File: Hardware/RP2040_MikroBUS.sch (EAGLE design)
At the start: 76 parts, among them J1 SWD, J3 Qwiic, J5 USB C, J6 microSD, J9 MIKROBUS_SMD_BLACK1, Q1 20V/4.2A/52mΩ/1.4W, U2 MAX17048, U3 MCP73831, U4 W25QXX128MBIT, U5 RP2040, U6 WS2812-2020, U7 3.3V, Y2 12MHz

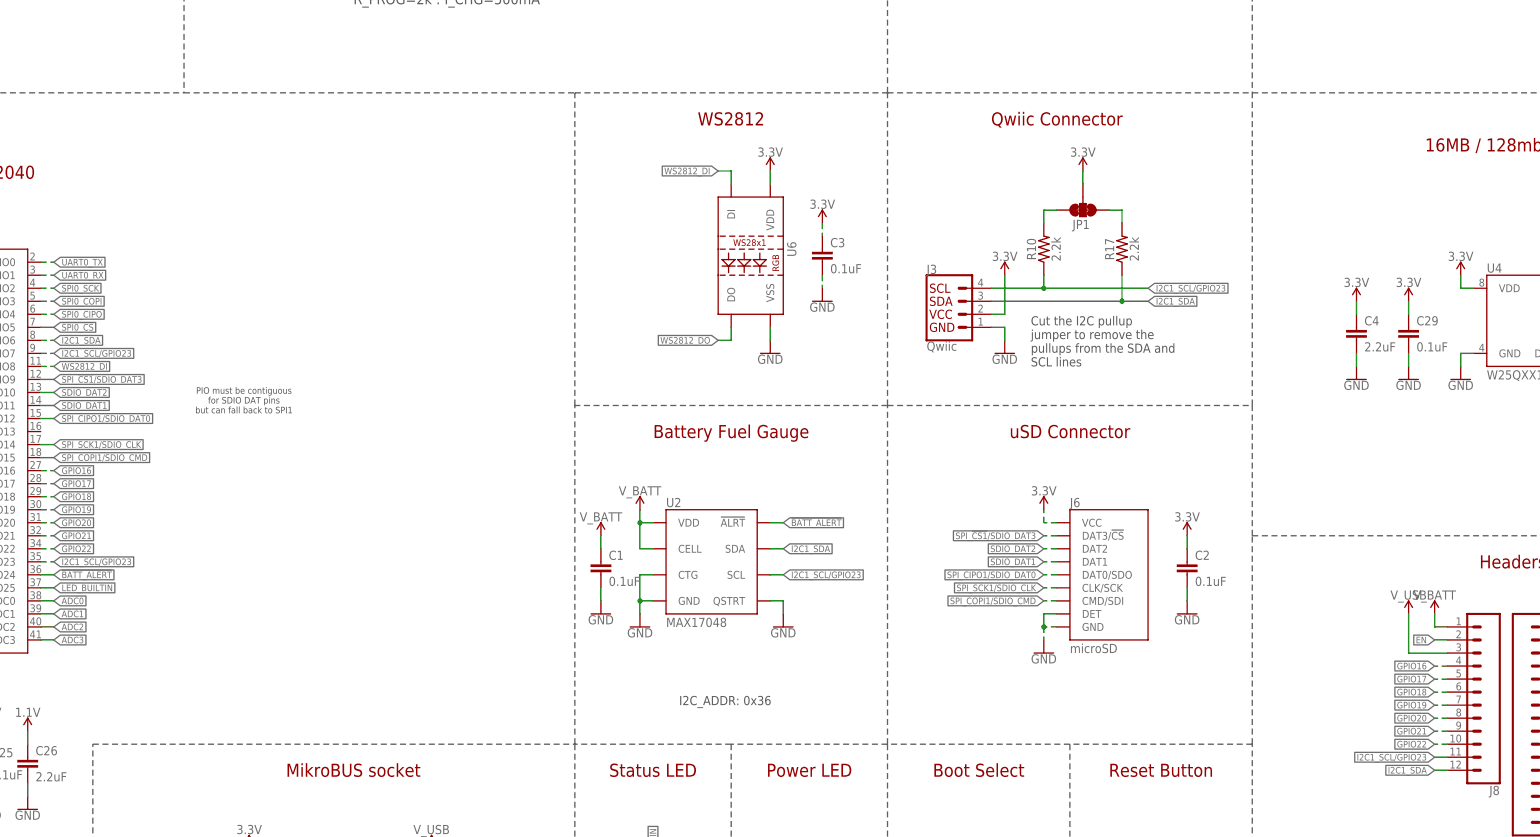
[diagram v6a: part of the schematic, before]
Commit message: Board updates
* Fix RESET button label
* Add RP2040 to SF microcontroller library and update in sch/board
* Gave some more space between the new traces I placed
* Brought D+ and D- traces closer together
* Changed "WS2812" label to text only
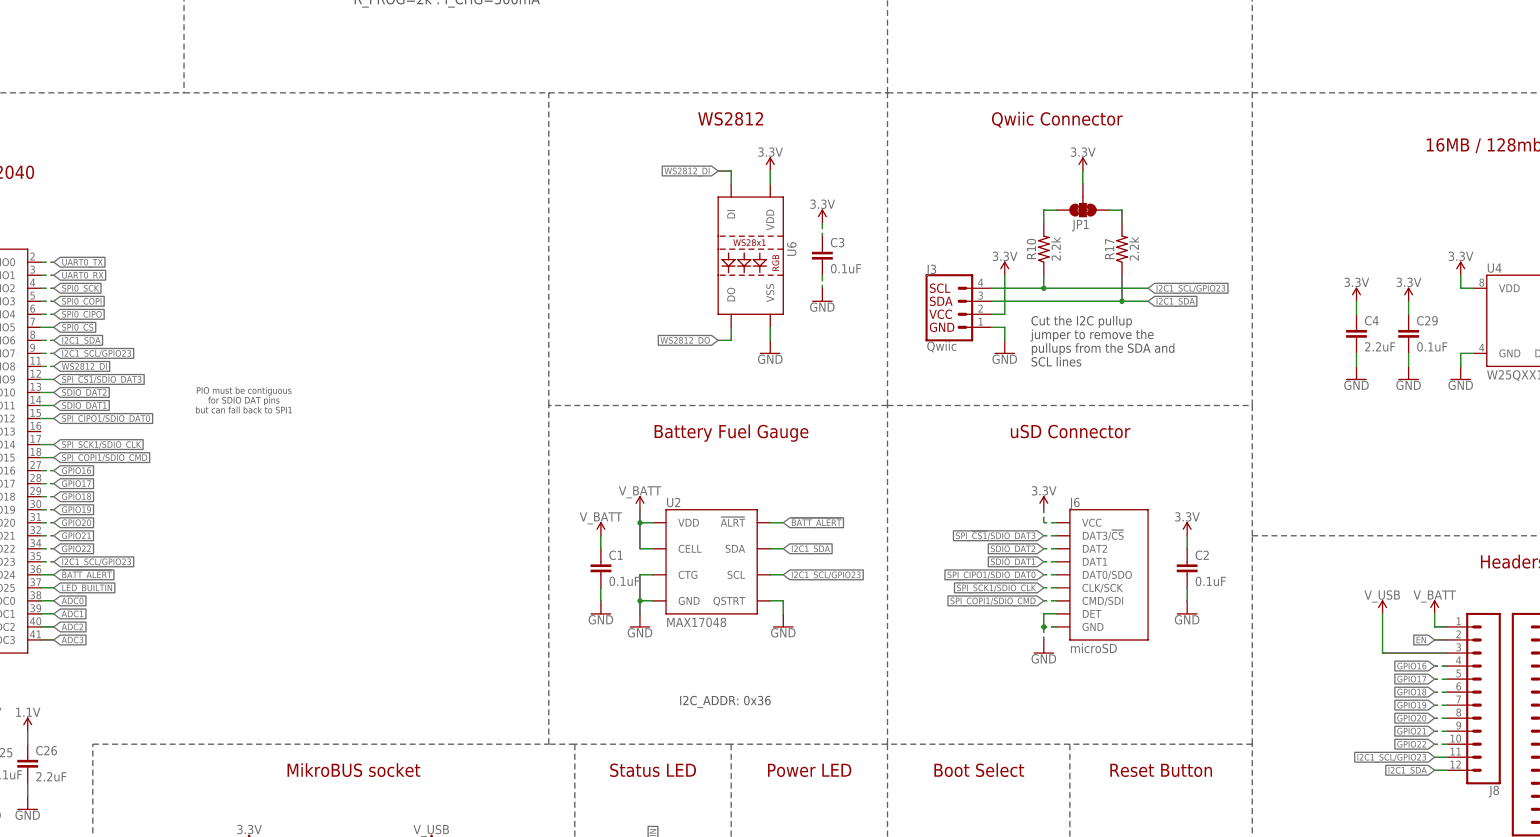
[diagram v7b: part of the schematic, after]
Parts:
- U5: device RP2040:RP2040 -> SparkFun-IC-Microcontroller:RP2040
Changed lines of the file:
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@@
 <part name="C16" library="SparkFun-Capacitors" deviceset="15PF" device="-0402T-50V-5%" value="15pF"/>
 <part name="GND35" library="SparkFun-PowerSymbols" deviceset="GND" device=""/>
-<part name="U5" library="RP2040" deviceset="RP2040" device=""/>
+<part name="U5" library="SparkFun-IC-Microcontroller" deviceset="RP2040" device=""/>
 <part name="GND5" library="SparkFun-PowerSymbols" deviceset="GND" device=""/>
 <part name="R11" library="SparkFun-Resistors" deviceset="1KOHM" device="-0402T-1/16W-1%" value="1k"/>
@@
 <part name="R12" library="SparkFun-Resistors" deviceset="27OHM" device="" value="27"/>
 <part name="R13" library="SparkFun-Resistors" deviceset="27OHM" device="" value="27"/>
-<part name="SUPPLY29" library="RP2040" deviceset="1.1V" device=""/>
-<part name="SUPPLY30" library="RP2040" deviceset="1.1V" device=""/>
-<part name="SUPPLY31" library="RP2040" deviceset="1.1V" device=""/>
+<part name="SUPPLY29" library="SparkFun-PowerSymbols" deviceset="1.1V" device=""/>
+<part name="SUPPLY30" library="SparkFun-PowerSymbols" deviceset="1.1V" device=""/>
+<part name="SUPPLY31" library="SparkFun-PowerSymbols" deviceset="1.1V" device=""/>
 <part name="C26" library="SparkFun-Capacitors" deviceset="2.2UF" device="-0402_TIGHT-10V-10%-X5R" value="2.2uF"/>
 <part name="C27" library="SparkFun-Capacitors" deviceset="2.2UF" device="-0402_TIGHT-10V-10%-X5R" value="2.2uF"/>
 <part name="SUPPLY32" library="SparkFun-PowerSymbols" deviceset="3.3V" device=""/>
-<part name="SUPPLY33" library="RP2040" deviceset="1.1V" device=""/>
+<part name="SUPPLY33" library="SparkFun-PowerSymbols" deviceset="1.1V" device=""/>
 <part name="GND27" library="SparkFun-PowerSymbols" deviceset="GND" device=""/>
 <part name="GND29" library="SparkFun-PowerSymbols" deviceset="GND" device=""/>
@@
 <wire x1="121.92" y1="279.4" x2="121.92" y2="193.04" width="0.2032" layer="97" style="longdash"/>
 <wire x1="330.2" y1="279.4" x2="330.2" y2="193.04" width="0.2032" layer="97" style="longdash"/>
-<wire x1="198.12" y1="66.04" x2="198.12" y2="0" width="0.2032" layer="97" style="longdash"/>
 <wire x1="330.2" y1="35.56" x2="330.2" y2="66.04" width="0.2032" layer="97" style="longdash"/>
 <wire x1="330.2" y1="66.04" x2="330.2" y2="106.68" width="0.2032" layer="97" style="longdash"/>
@@
 <wire x1="259.08" y1="66.04" x2="228.6" y2="66.04" width="0.2032" layer="97" style="longdash"/>
 <wire x1="228.6" y1="66.04" x2="198.12" y2="66.04" width="0.2032" layer="97" style="longdash"/>
+<wire x1="198.12" y1="66.04" x2="193.04" y2="66.04" width="0.2032" layer="97" style="longdash"/>
 <wire x1="259.08" y1="66.04" x2="259.08" y2="132.08" width="0.1524" layer="97" style="longdash"/>
 <wire x1="259.08" y1="132.08" x2="259.08" y2="193.04" width="0.1524" layer="97" style="longdash"/>
 <wire x1="259.08" y1="132.08" x2="330.2" y2="132.08" width="0.1524" layer="97" style="longdash"/>
-<wire x1="121.92" y1="193.04" x2="198.12" y2="193.04" width="0.1524" layer="97" style="longdash"/>
+<wire x1="121.92" y1="193.04" x2="193.04" y2="193.04" width="0.1524" layer="97" style="longdash"/>
 <text x="287.02" y="139.7" size="1.778" layer="97" font="vector">Cut the I2C pullup
 jumper to remove the
@@
 for SDIO DAT pins
 but can fall back to SPI1</text>
-<wire x1="198.12" y1="193.04" x2="259.08" y2="193.04" width="0.1524" layer="97" style="longdash"/>
-<wire x1="198.12" y1="66.04" x2="198.12" y2="132.08" width="0.2032" layer="97" style="longdash"/>
-<wire x1="198.12" y1="132.08" x2="198.12" y2="193.04" width="0.2032" layer="97" style="longdash"/>
-<wire x1="259.08" y1="132.08" x2="198.12" y2="132.08" width="0.2032" layer="97" style="longdash"/>
+<wire x1="193.04" y1="193.04" x2="259.08" y2="193.04" width="0.1524" layer="97" style="longdash"/>
+<wire x1="193.04" y1="66.04" x2="193.04" y2="132.08" width="0.2032" layer="97" style="longdash"/>
+<wire x1="193.04" y1="132.08" x2="193.04" y2="193.04" width="0.2032" layer="97" style="longdash"/>
+<wire x1="259.08" y1="132.08" x2="193.04" y2="132.08" width="0.2032" layer="97" style="longdash"/>
 <text x="381" y="182.88" size="2.54" layer="94" font="vector" align="center">16MB / 128mbit Flash</text>
 <text x="294.64" y="127" size="2.54" layer="94" font="vector" align="center">uSD Connector</text>
@@
 <text x="243.84" y="60.96" size="2.54" layer="94" font="vector" align="center">Power LED</text>
 <wire x1="104.14" y1="0" x2="104.14" y2="66.04" width="0.2032" layer="97" style="longdash"/>
-<wire x1="104.14" y1="66.04" x2="198.12" y2="66.04" width="0.2032" layer="97" style="longdash"/>
+<wire x1="104.14" y1="66.04" x2="193.04" y2="66.04" width="0.2032" layer="97" style="longdash"/>
 <text x="154.94" y="60.96" size="2.54" layer="94" font="vector" align="center">MikroBUS socket</text>
+<wire x1="198.12" y1="66.04" x2="198.12" y2="0" width="0.2032" layer="97" style="longdash"/>
 </plain>
 <instances>
@@
 <attribute name="VALUE" x="373.38" y="249.174" size="1.778" layer="96" align="bottom-center"/>
 </instance>
-<instance part="SUPPLY14" gate="G$1" x="360.68" y="91.44" smashed="yes">
-<attribute name="VALUE" x="360.68" y="94.234" size="1.778" layer="96" align="bottom-center"/>
+<instance part="SUPPLY14" gate="G$1" x="355.6" y="91.44" smashed="yes">
+<attribute name="VALUE" x="355.6" y="94.234" size="1.778" layer="96" align="bottom-center"/>
 </instance>
 <instance part="SUPPLY6" gate="G$1" x="48.26" y="251.46" smashed="yes">
@@
 </segment>
 <segment>
-<wire x1="360.68" y1="91.44" x2="360.68" y2="83.82" width="0.1524" layer="91"/>
-<wire x1="360.68" y1="83.82" x2="368.3" y2="83.82" width="0.1524" layer="91"/>
+<wire x1="355.6" y1="91.44" x2="355.6" y2="83.82" width="0.1524" layer="91"/>
+<wire x1="355.6" y1="83.82" x2="368.3" y2="83.82" width="0.1524" layer="91"/>
 <pinref part="J8" gate="G$1" pin="3"/>
 <pinref part="SUPPLY14" gate="G$1" pin="V_USB"/>

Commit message: Run checklist
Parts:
- removed U6: WS2812-2020, SparkFun-LED:WS2812-2020
- added D5: WS2812_2020, SparkFun-LED:WS2812_2020
- added LOGO1: OSHW-LOGOS, SparkFun-Aesthetics:OSHW-LOGOS
- added LOGO2: SFE_LOGO_NAME.1_INCH, SparkFun-Aesthetics:SFE_LOGO_NAME.1_INCH
- renumbered JP1 to I2C
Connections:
- net 3.3V: now also D5.VCC; no longer U6.VDD
- net GND: now also D5.GND; no longer U6.VSS
- net WS2812_DI: now also D5.DI; no longer U6.DI
- net WS2812_DO: now also D5.DO; no longer U6.DO
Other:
- note added: "Nick Poole"
- note added: "Revised by: Priyanka Makin"
- moved on the sheet: C16, C28, C3, C5, R11, R12, R13, R7, U5, Y2
